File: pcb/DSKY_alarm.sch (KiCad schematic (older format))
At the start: 87 parts, among them IC3 ATSAMD21E, J1 105133-0001-MOLEX-USB, SW1 reset, U1 AQY232SZ, U10 AQY232SZ, U11 AQY232SZ, U12 AQY232SZ, U13 AQY232SZ, U14 AQY232SZ, U15 AP2112K-3.3, U2 AQY232SZ, U3 AQY232SZ, U4 AQY232SZ, U5 AQY232SZ, U6 AQY232SZ, U7 AQY232SZ, U8 AQY232SZ, u9 AQY232SZ

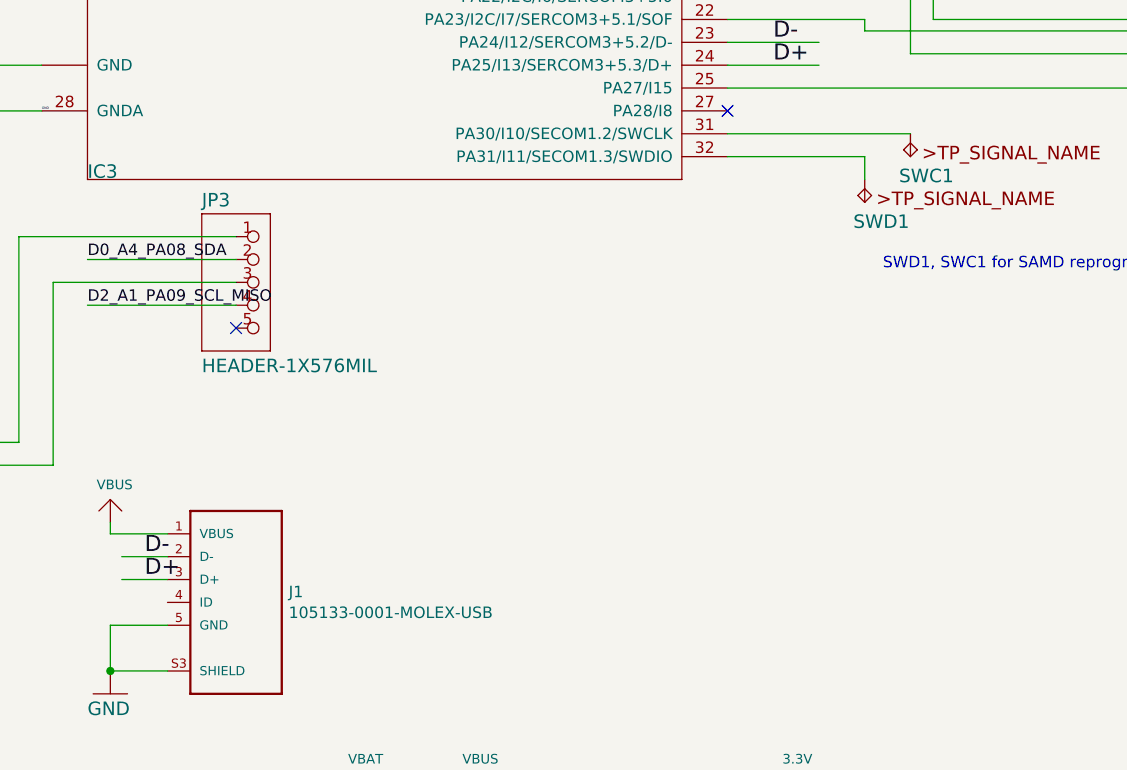
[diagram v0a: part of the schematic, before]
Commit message: Cleanup of schematic files
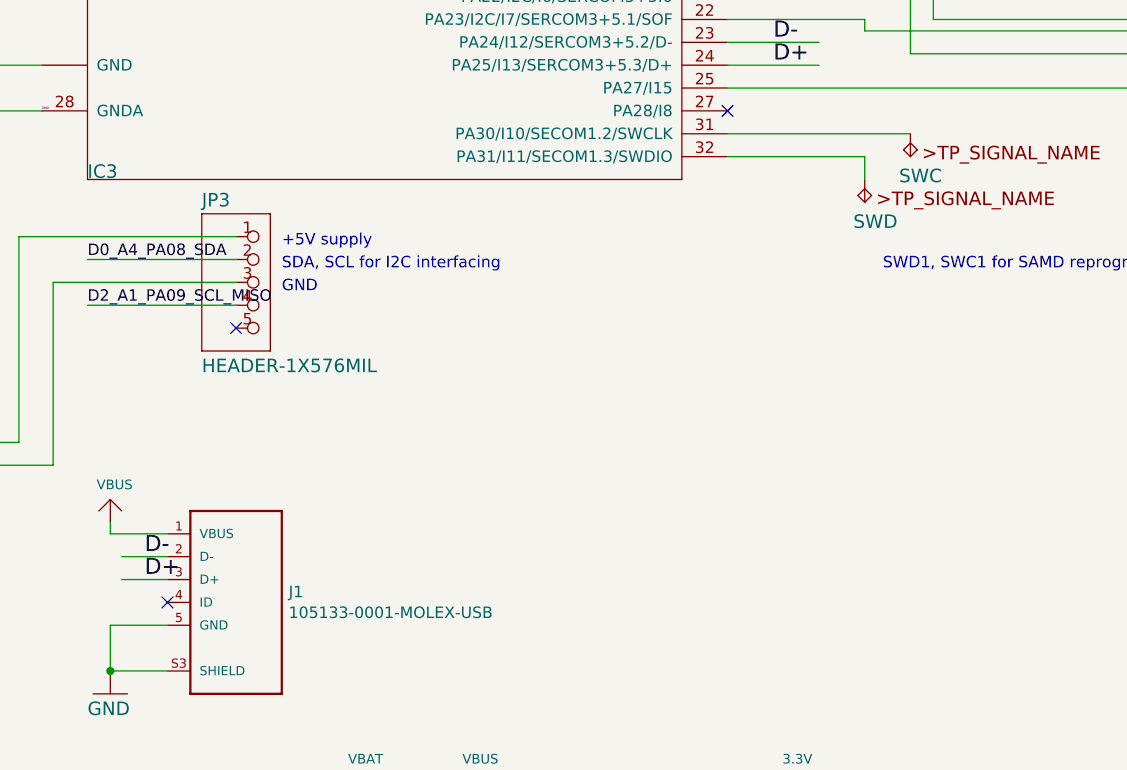
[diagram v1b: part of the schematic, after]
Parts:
- renumbered SWC1 to SWC, SWD1 to SWD
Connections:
- no-connect marks 5 -> 6
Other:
- note added: "+5V supply"
- note added: "GND\n"
- note added: "SDA, SCL for I2C interfacing"
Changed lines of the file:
@@
 Rev "4"
 Comp ""
-Comment1 ""
-Comment2 ""
+Comment1 "Design by Riley Rainey"
+Comment2 "Elements based on Adafruit Trinket M0"
 Comment3 ""
 Comment4 ""
@@
 $EndComp
 $Comp
-L Trinket_M0_rev_D-eagle-import:TPB1,27 SWC1
+L Trinket_M0_rev_D-eagle-import:TPB1,27 SWC
 U 1 1 7F04099A
 P 6200 4900
-F 0 "SWC1" H 6150 4950 59  0000 L BNN
+F 0 "SWC" H 6150 4950 59  0000 L BNN
 F 1 "TPB1,27" H 6200 4900 50  0001 C CNN
 F 2 "Trinket M0 rev D:B1,27" H 6200 4900 50  0001 C CNN
@@
 $EndComp
 $Comp
-L Trinket_M0_rev_D-eagle-import:TPB1,27 SWD1
+L Trinket_M0_rev_D-eagle-import:TPB1,27 SWD
 U 1 1 87123050
 P 6000 5100
-F 0 "SWD1" H 5950 5150 59  0000 L BNN
+F 0 "SWD" H 5950 5150 59  0000 L BNN
 F 1 "TPB1,27" H 6000 5100 50  0001 C CNN
 F 2 "Trinket M0 rev D:B1,27" H 6000 5100 50  0001 C CNN
@@
 Wire Wire Line
 	2700 6550 2700 6500
+NoConn ~ 2950 6850
+Text Notes 3450 5400 0    50   ~ 0
+SDA, SCL for I2C interfacing
+Text Notes 3450 5300 0    50   ~ 0
++5V supply
+Text Notes 3450 5500 0    50   ~ 0
+GND\n
 $EndSCHEMATC
